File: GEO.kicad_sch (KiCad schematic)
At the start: 11 parts, among them J2 Screw_Terminal_01x02

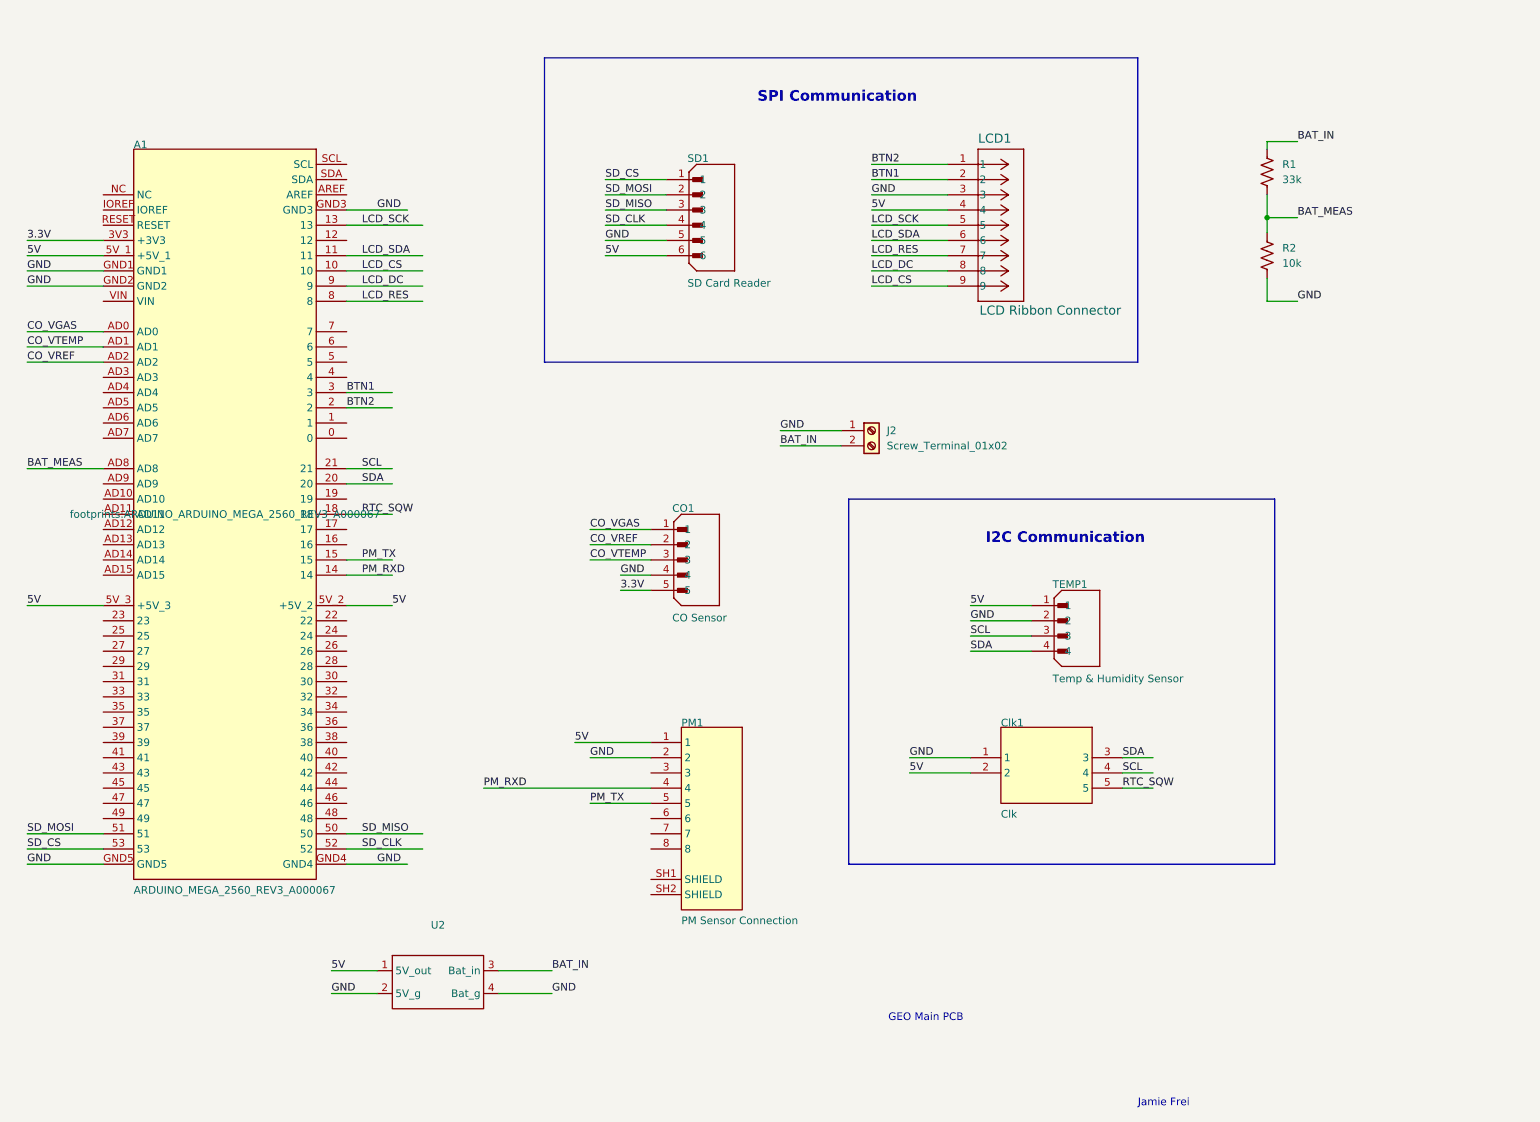
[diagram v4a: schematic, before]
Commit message: cleaned up the schematic
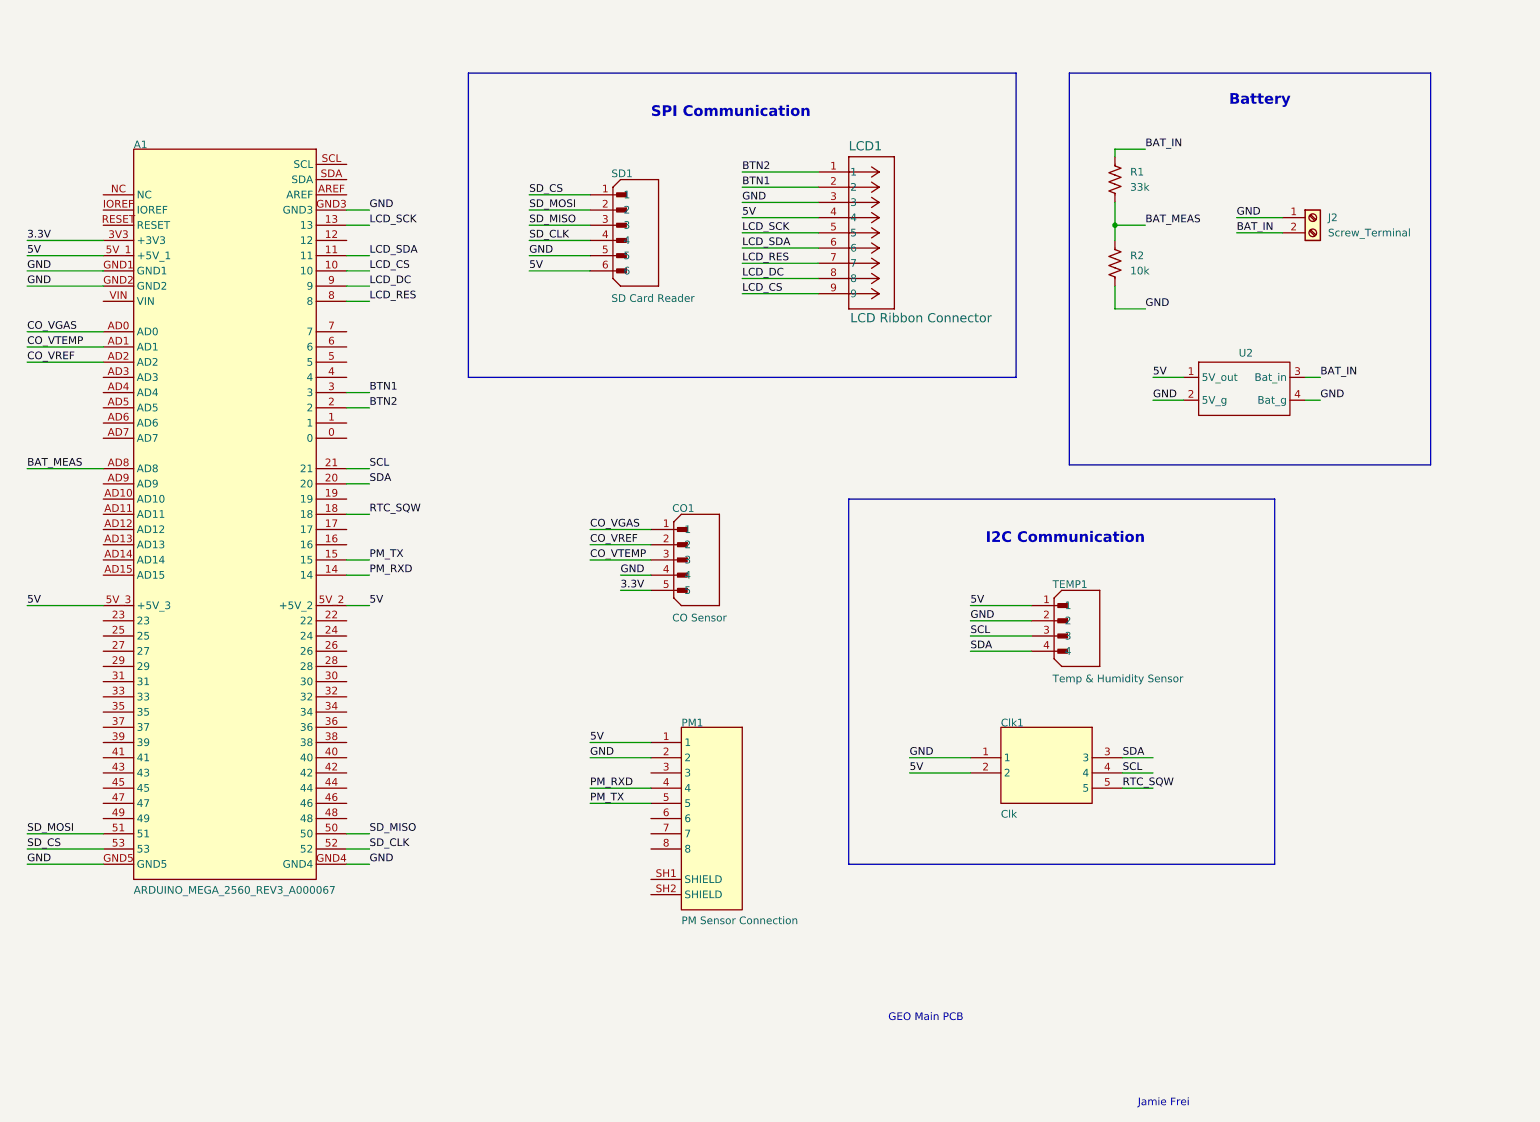
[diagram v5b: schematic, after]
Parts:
- J2: value Screw_Terminal_01x02 -> Screw_Terminal
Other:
- note added: "Battery"
- moved on the sheet: J2, LCD1, R1, R2, SD1, U2
